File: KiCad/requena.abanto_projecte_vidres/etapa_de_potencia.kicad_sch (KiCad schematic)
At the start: 0 parts

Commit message: avance etapa de potencia
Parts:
- added C1: 1000 uF, symbol Device:C_Polarized
- added C2: 100n, symbol Device:C
- added R-SHUNT: 10m, symbol Device:R
- added R1, R2: 10k, symbol Device:R
- added R3, R4, R5: 1k, symbol Device:R
- added U1: VNH5019A-E, Package_SO:ST_MultiPowerSO-30, symbol Driver_Motor:VNH5019A-E
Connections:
- new net: R5.2, U1.10 (INB)
- new net: R3.2, U1.7 (PWM)
- new net: R2.1, U1.9 (EN/DIAGB)
- new net: R4.2, U1.4 (INA)
- new net: R1.1, U1.5 (EN/DIAGA)
- new net GND: C1.2, C2.2, R-SHUNT.1, U1.6 (CS_DIS)
- new net INA: R4.1
- new net INB: R5.1
- new net MOTOR_A: U1.1 (OUTA), U1.25 (OUTA), U1.30 (OUTA), U1.33 (OUTA)
- new net MOTOR_B: U1.15 (OUTB), U1.16 (OUTB), U1.21 (OUTB), U1.32 (OUTB)
- new net PIN_DIGITAL1: R1.2, R2.2
- new net PWM: R3.1
- new net V_BAT: C1.1, C2.1, U1.12 (VBAT), U1.13 (VCC), U1.23 (VCC), U1.3 (VCC), U1.31 (VCC)
- new net V_SHUNT: R-SHUNT.2, U1.18 (GNDB), U1.19 (GNDB), U1.20 (GNDB), U1.26 (GNDA), U1.27 (GNDA), U1.28 (GNDA)
- no-connect marks 0 -> 2
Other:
- note added: "A RBxx"
- note added: "A RBxx A RBxx"

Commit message: arreglos
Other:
- note removed: "A RBxx"
- note removed: "A RBxx A RBxx"
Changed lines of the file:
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@@
 	(generator_version "9.0")
 	(paper "A4")
-	(text "A RBxx\n"
-		(exclude_from_sim no)
-		(at 79.248 65.024 0)
-		(effects
-			(font
-				(size 1.27 1.27)
-			)
-		)
-	)
-	(text "A RBxx\n"
-		(exclude_from_sim no)
-		(at 78.486 56.388 0)
-		(effects
-			(font
-				(size 1.27 1.27)
-			)
-		)
-	)
-	(text "A RBxx\n"
-		(exclude_from_sim no)
-		(at 77.978 59.436 0)
-		(effects
-			(font
-				(size 1.27 1.27)
-			)
-		)
-	)
-	(text "A RBxx\nA RBxx\n"
-		(exclude_from_sim no)
-		(at 209.042 62.23 0)
-		(effects
-			(font
-				(size 1.27 1.27)
-			)
-		)
-	)
 	(junction
 		(at 138.43 78.74)

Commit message: saywallahibro,canvis
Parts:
- added C3, C4: 100n, symbol Device:C
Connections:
- net GND: now also C3.2
- net PIN_DIGITAL1: now also U1.13 (VCC), U1.23 (VCC), U1.3 (VCC), U1.31 (VCC), C3.1
- net V_BAT: now also C4.2; no longer U1.13 (VCC), U1.23 (VCC), U1.3 (VCC), U1.31 (VCC)
- net at U1.11 (CP): now also C4.1
- no-connect marks 2 -> 1
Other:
- moved on the sheet: C1, C2

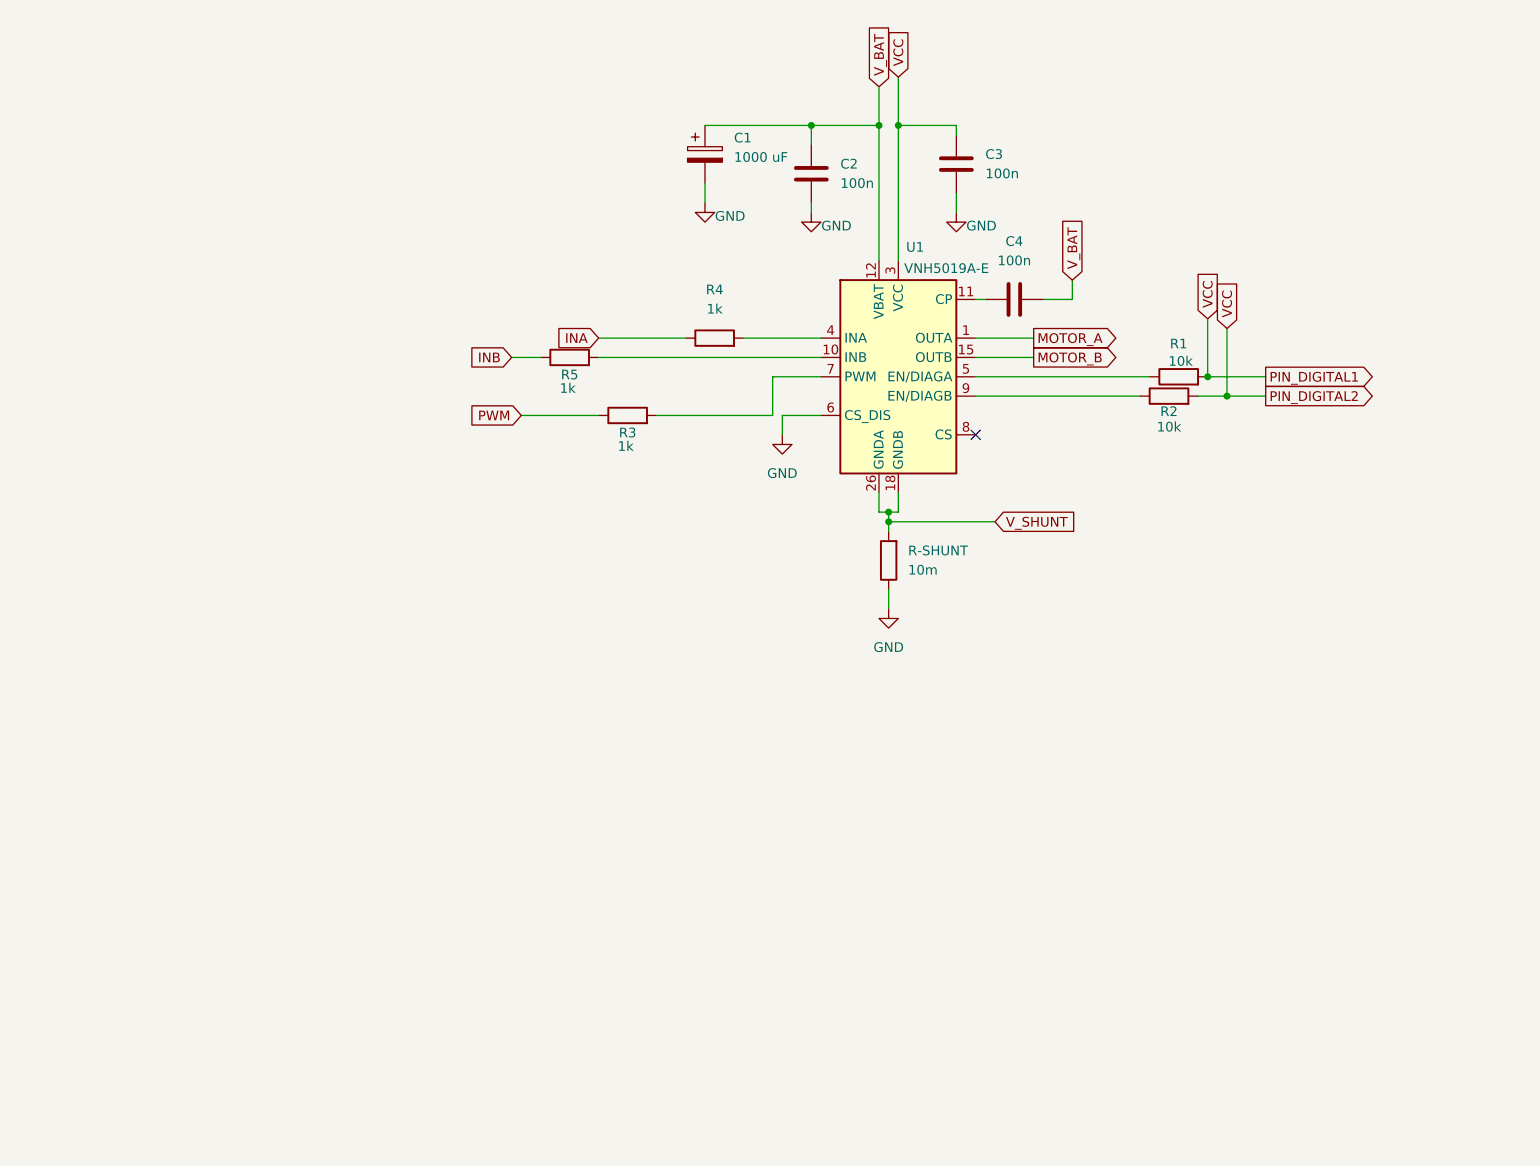
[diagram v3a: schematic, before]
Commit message: millora el esquematic
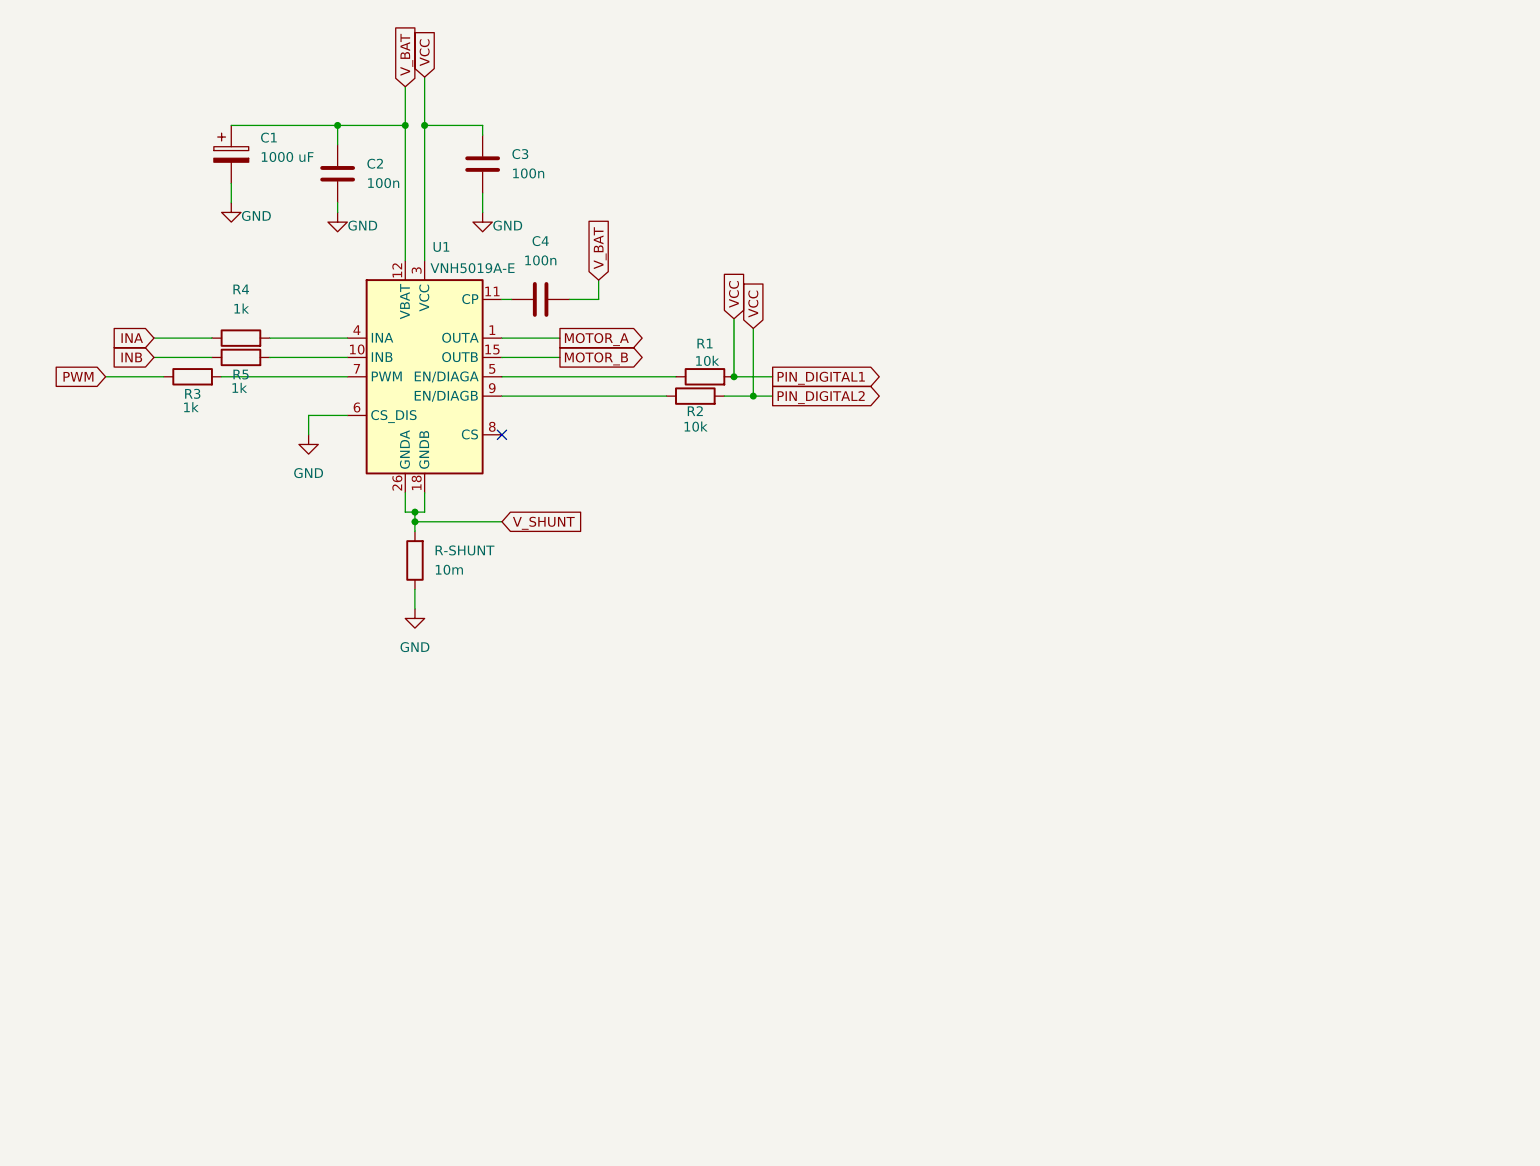
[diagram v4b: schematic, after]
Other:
- moved on the sheet: C1, C2, C3, C4, R-SHUNT, R1, R2, R3, R4, R5, U1

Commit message: Millora projecte 1
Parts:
- removed C1: 1000 uF, symbol Device:C_Polarized
- removed C2, C3, C4: 100n, symbol Device:C
- removed R-SHUNT: 10m, symbol Device:R
- removed R1, R2: 10k, symbol Device:R
- removed R3, R4, R5: 1k, symbol Device:R
- removed U1: VNH5019A-E, Package_SO:ST_MultiPowerSO-30, symbol Driver_Motor:VNH5019A-E
- added C1, C9: 100n, symbol Device:C
- added C5, C8: 100nF, symbol Device:C
- added C6, C7: 1uF, symbol Device:C_Polarized
- added D1: D, symbol Device:D
- added D2: D_Zener, symbol Device:D_Zener
- added R6, R7: R, symbol Device:R
- added R8: R_Shunt, symbol Device:R_Shunt
- added U2: LM1117DT-3.3, Package_TO_SOT_SMD:TO-252-3_TabPin2, symbol Regulator_Linear:LM1117DT-3.3
- added U2: TSR2-2450, Converter_DCDC:Converter_DCDC_TRACO_TSR2-xxxx_THT, symbol Converter_DCDC:TSR2-2450
- added U3: MCP6001-OT, Package_TO_SOT_SMD:SOT-23-5, symbol Amplifier_Operational:MCP6001-OT
- added U4: L298N, Package_TO_SOT_THT:TO-220-15_P2.54x5.08mm_StaggerOdd_Lead4.58mm_Vertical, symbol Driver_Motor:L298N
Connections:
- net GND: now also C1.1, C5.2, C6.2, C7.2, C8.2, C9.2, D2.2 (A), R6.1, R8.3, R8.4, U2.1 (GND), U2.2 (GND), U3.2 (V-), U4.1 (SENSE_A), U4.15 (SENSE_B)
- net INA: now also U4.5 (IN1)
- net INB: now also U4.7 (IN2)
- net PWM: now also U4.6 (EnA)
- new net: C5.1, C6.1, D1.1 (K), D2.1 (K), U2.1 (Vin)
- new net: R6.2, R7.1, U3.4 (-)
- new net: R8.1, U4.8 (GND)
- new net: R8.2, U3.3 (+)
- new net +12V: D1.2 (A), U4.4 (Vs)
- new net AN0: R7.2, U3.1
- new net VCC: C1.2, C7.1, C8.1, C9.1, U2.2 (VO), U3.5 (V+), U4.9 (Vss)
- new net V_OUT_DCDC: U2.3 (VI), U2.3 (Vout)
- no-connect marks 1 -> 3

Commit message: cambios
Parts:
- removed U3: MCP6001-OT, Package_TO_SOT_SMD:SOT-23-5, symbol Amplifier_Operational:MCP6001-OT
- added U1: MCP6022, symbol Amplifier_Operational:MCP6022
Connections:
- net AN0: now also R7.1, U1.1, U1.5 (+), U1.7; no longer R7.2
- net GND: now also U1.4 (V-), U1.6 (-)
- net VCC: now also U1.8 (V+)
- net at R6.2: now also R7.2, U1.2 (-); no longer R7.1
- net at R8.2: now also U1.3 (+)
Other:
- moved on the sheet: C1, C5, C6, C7, C8, C9, D1, D2, R6, R7, R8, U2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

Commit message: correcions
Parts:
- removed U1: MCP6022, symbol Amplifier_Operational:MCP6022
- added U3: MCP6022, symbol Amplifier_Operational:MCP6022
- renumbered C5 to C1, C1 to C2, C6 to C3, C7 to C4, C8 to C5, C9 to C6, R8 to R1, R6 to R2, R7 to R3, U4 to U1, U2 to U4
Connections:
- net AN0: now also U3.1, U3.5 (+), U3.7
- net GND: now also U3.4 (V-), U3.6 (-)
- net VCC: now also U3.8 (V+)
- net at R2.2, R3.2: now also U3.2 (-)
- net at R1.2: now also U3.3 (+)
